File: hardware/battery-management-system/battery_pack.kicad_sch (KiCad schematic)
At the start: 24 parts, among them J1 CELLS, J2 Charge, J3 Discharge, J4 VBAT_DISCHARGE, Q1 DMN3404L, Q2 TJ40S04M3L, Q3 TJ40S04M3L, Q4 DMN3404L, U11 STC3100

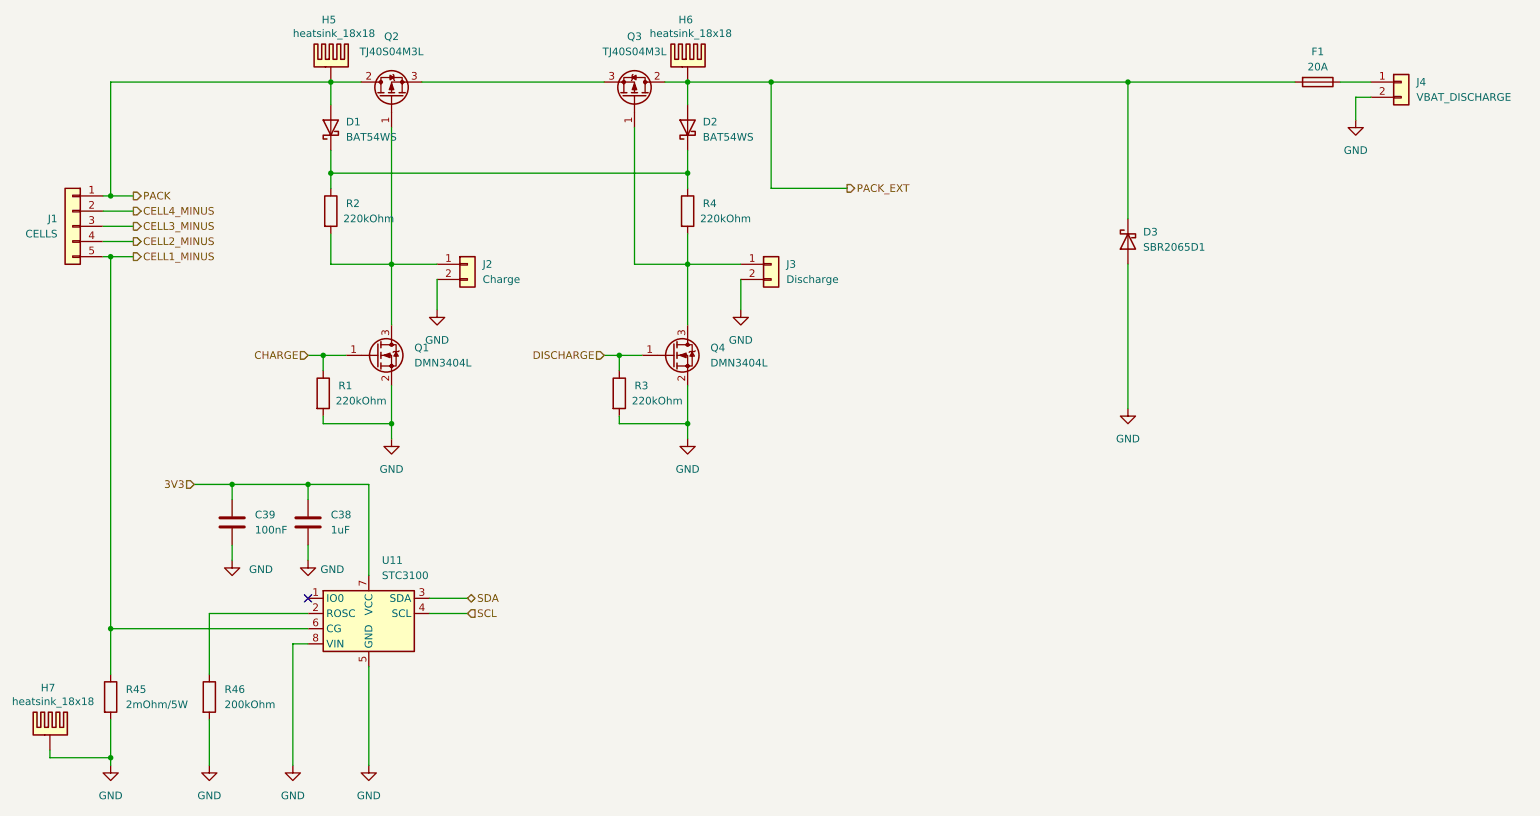
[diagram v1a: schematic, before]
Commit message: add snubber circuit
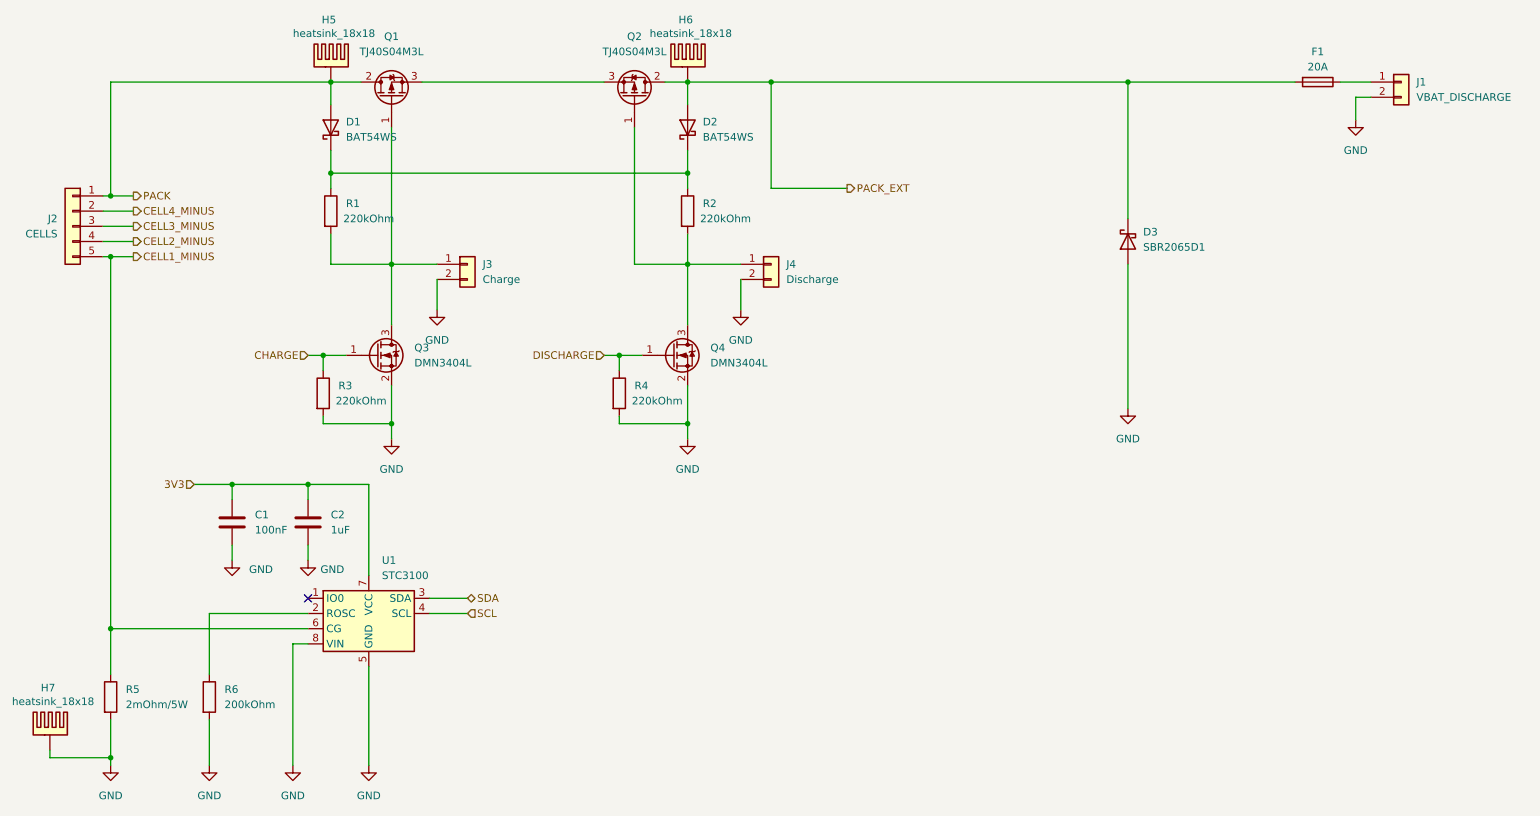
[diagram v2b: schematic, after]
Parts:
- renumbered C39 to C1, C38 to C2, J4 to J1, J1 to J2, J2 to J3, J3 to J4, Q2 to Q1, Q3 to Q2, Q1 to Q3, R2 to R1, R4 to R2, R1 to R3, R3 to R4, R45 to R5, R46 to R6, U11 to U1
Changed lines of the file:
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@@
 		(dnp no)
 		(fields_autoplaced yes)
-		(property "Reference" "J4"
+		(property "Reference" "J1"
 			(at 266.7 44.45 0)
 			(effects
@@
 			(project "battery-management-system"
 				(path "/5272f0ff-3069-41a9-bca2-80beede8b4b2/31b87c35-c096-4dc0-8978-834bec283b57"
-					(reference "J4")
+					(reference "J1")
 					(unit 1)
 				)
@@
 		(dnp no)
 		(fields_autoplaced yes)
-		(property "Reference" "#PWR09"
+		(property "Reference" "#PWR07"
 			(at 153.67 88.9 0)
 			(effects
@@
 			(project "battery-management-system"
 				(path "/5272f0ff-3069-41a9-bca2-80beede8b4b2/31b87c35-c096-4dc0-8978-834bec283b57"
-					(reference "#PWR09")
+					(reference "#PWR07")
 					(unit 1)
 				)
@@
 		(dnp no)
 		(fields_autoplaced yes)
-		(property "Reference" "#PWR071"
+		(property "Reference" "#PWR08"
 			(at 218.44 105.41 0)
 			(effects
@@
 			(project "battery-management-system"
 				(path "/5272f0ff-3069-41a9-bca2-80beede8b4b2/31b87c35-c096-4dc0-8978-834bec283b57"
-					(reference "#PWR071")
+					(reference "#PWR08")
 					(unit 1)
 				)
@@
 		(dnp no)
 		(fields_autoplaced yes)
-		(property "Reference" "C39"
+		(property "Reference" "C1"
 			(at 72.39 116.8399 0)
 			(effects
@@
 			(project "battery-management-system"
 				(path "/5272f0ff-3069-41a9-bca2-80beede8b4b2/31b87c35-c096-4dc0-8978-834bec283b57"
-					(reference "C39")
+					(reference "C1")
 					(unit 1)
 				)
@@
 		(dnp no)
 		(fields_autoplaced yes)
-		(property "Reference" "J2"
+		(property "Reference" "J3"
 			(at 110.49 74.93 0)
 			(effects
@@
 			(project "battery-management-system"
 				(path "/5272f0ff-3069-41a9-bca2-80beede8b4b2/31b87c35-c096-4dc0-8978-834bec283b57"
-					(reference "J2")
+					(reference "J3")
 					(unit 1)
 				)
@@
 		(on_board yes)
 		(dnp no)
-		(property "Reference" "R3"
+		(property "Reference" "R4"
 			(at 135.89 95.2499 0)
 			(effects
@@
 			(project "battery-management-system"
 				(path "/5272f0ff-3069-41a9-bca2-80beede8b4b2/31b87c35-c096-4dc0-8978-834bec283b57"
-					(reference "R3")
+					(reference "R4")
 					(unit 1)
 				)
@@
 		(dnp no)
 		(fields_autoplaced yes)
-		(property "Reference" "U11"
+		(property "Reference" "U1"
 			(at 93.6341 124.46 0)
 			(effects
@@
 			(project "battery-management-system"
 				(path "/5272f0ff-3069-41a9-bca2-80beede8b4b2/31b87c35-c096-4dc0-8978-834bec283b57"
-					(reference "U11")
+					(reference "U1")
 					(unit 1)
 				)
@@
 		(dnp no)
 		(fields_autoplaced yes)
-		(property "Reference" "#PWR08"
+		(property "Reference" "#PWR010"
 			(at 144.78 110.49 0)
 			(effects
@@
 			(project "battery-management-system"
 				(path "/5272f0ff-3069-41a9-bca2-80beede8b4b2/31b87c35-c096-4dc0-8978-834bec283b57"
-					(reference "#PWR08")
+					(reference "#PWR010")
 					(unit 1)
 				)
@@
 		(on_board yes)
 		(dnp no)
-		(property "Reference" "R46"
+		(property "Reference" "R6"
 			(at 67.31 146.0499 0)
 			(effects
@@
 			(project "battery-management-system"
 				(path "/5272f0ff-3069-41a9-bca2-80beede8b4b2/31b87c35-c096-4dc0-8978-834bec283b57"
-					(reference "R46")
+					(reference "R6")
 					(unit 1)
 				)
@@
 		(dnp no)
 		(fields_autoplaced yes)
-		(property "Reference" "#PWR06"
+		(property "Reference" "#PWR09"
 			(at 95.25 110.49 0)
 			(effects
@@
 			(project "battery-management-system"
 				(path "/5272f0ff-3069-41a9-bca2-80beede8b4b2/31b87c35-c096-4dc0-8978-834bec283b57"
-					(reference "#PWR06")
+					(reference "#PWR09")
 					(unit 1)
 				)
@@
 		(dnp no)
 		(fields_autoplaced yes)
-		(property "Reference" "R45"
+		(property "Reference" "R5"
 			(at 50.8 146.0499 0)
 			(effects
@@
 			(project "battery-management-system"
 				(path "/5272f0ff-3069-41a9-bca2-80beede8b4b2/31b87c35-c096-4dc0-8978-834bec283b57"
-					(reference "R45")
+					(reference "R5")
 					(unit 1)
 				)
@@
 		(dnp no)
 		(fields_autoplaced yes)
-		(property "Reference" "#PWR05"
+		(property "Reference" "#PWR013"
 			(at 48.26 165.1 0)
 			(effects
@@
 			(project "battery-management-system"
 				(path "/5272f0ff-3069-41a9-bca2-80beede8b4b2/31b87c35-c096-4dc0-8978-834bec283b57"
-					(reference "#PWR05")
+					(reference "#PWR013")
 					(unit 1)
 				)
@@
 		(on_board yes)
 		(dnp no)
-		(property "Reference" "J1"
+		(property "Reference" "J2"
 			(at 39.37 67.31 0)
 			(effects
@@
 			(project "battery-management-system"
 				(path "/5272f0ff-3069-41a9-bca2-80beede8b4b2/31b87c35-c096-4dc0-8978-834bec283b57"
-					(reference "J1")
+					(reference "J2")
 					(unit 1)
 				)
@@
 		(on_board yes)
 		(dnp no)
-		(property "Reference" "R2"
+		(property "Reference" "R1"
 			(at 87.63 64.7699 0)
 			(effects
@@
 			(project "battery-management-system"
 				(path "/5272f0ff-3069-41a9-bca2-80beede8b4b2/31b87c35-c096-4dc0-8978-834bec283b57"
-					(reference "R2")
+					(reference "R1")
 					(unit 1)
 				)
@@
 		(dnp no)
 		(fields_autoplaced yes)
-		(property "Reference" "#PWR073"
+		(property "Reference" "#PWR014"
 			(at 64.77 165.1 0)
 			(effects
@@
 			(project "battery-management-system"
 				(path "/5272f0ff-3069-41a9-bca2-80beede8b4b2/31b87c35-c096-4dc0-8978-834bec283b57"
-					(reference "#PWR073")
+					(reference "#PWR014")
 					(unit 1)
 				)
@@
 		(dnp no)
 		(fields_autoplaced yes)
-		(property "Reference" "C38"
+		(property "Reference" "C2"
 			(at 85.09 116.8399 0)
 			(effects
@@
 			(project "battery-management-system"
 				(path "/5272f0ff-3069-41a9-bca2-80beede8b4b2/31b87c35-c096-4dc0-8978-834bec283b57"
-					(reference "C38")
+					(reference "C2")
 					(unit 1)
 				)
@@
 		(dnp no)
 		(fields_autoplaced yes)
-		(property "Reference" "Q3"
+		(property "Reference" "Q2"
 			(at 135.89 36.83 90)
 			(effects
@@
 			(project "battery-management-system"
 				(path "/5272f0ff-3069-41a9-bca2-80beede8b4b2/31b87c35-c096-4dc0-8978-834bec283b57"
-					(reference "Q3")
+					(reference "Q2")
 					(unit 1)
 				)
@@
 		(dnp no)
 		(fields_autoplaced yes)
-		(property "Reference" "#PWR075"
+		(property "Reference" "#PWR016"
 			(at 91.44 165.1 0)
 			(effects
@@
 			(project "battery-management-system"
 				(path "/5272f0ff-3069-41a9-bca2-80beede8b4b2/31b87c35-c096-4dc0-8978-834bec283b57"
-					(reference "#PWR075")
+					(reference "#PWR016")
 					(unit 1)
 				)
@@
 		(dnp no)
 		(fields_autoplaced yes)
-		(property "Reference" "Q2"
+		(property "Reference" "Q1"
 			(at 95.25 36.83 90)
 			(effects
@@
 			(project "battery-management-system"
 				(path "/5272f0ff-3069-41a9-bca2-80beede8b4b2/31b87c35-c096-4dc0-8978-834bec283b57"
-					(reference "Q2")
+					(reference "Q1")
 					(unit 1)
 				)
@@
 		(on_board yes)
 		(dnp no)
-		(property "Reference" "R4"
+		(property "Reference" "R2"
 			(at 147.32 64.7699 0)
 			(effects
@@
 			(project "battery-management-system"
 				(path "/5272f0ff-3069-41a9-bca2-80beede8b4b2/31b87c35-c096-4dc0-8978-834bec283b57"
-					(reference "R4")
+					(reference "R2")
 					(unit 1)
 				)
@@
 		(dnp no)
 		(fields_autoplaced yes)
-		(property "Reference" "#PWR012"
+		(property "Reference" "#PWR05"
 			(at 256.54 57.15 0)
 			(effects
@@
 			(project "battery-management-system"
 				(path "/5272f0ff-3069-41a9-bca2-80beede8b4b2/31b87c35-c096-4dc0-8978-834bec283b57"
-					(reference "#PWR012")
+					(reference "#PWR05")
 					(unit 1)
 				)
@@
 		(on_board yes)
 		(dnp no)
-		(property "Reference" "#PWR076"
+		(property "Reference" "#PWR012"
 			(at 81.28 130.81 0)
 			(effects
@@
 			(project "battery-management-system"
 				(path "/5272f0ff-3069-41a9-bca2-80beede8b4b2/31b87c35-c096-4dc0-8978-834bec283b57"
-					(reference "#PWR076")
+					(reference "#PWR012")
 					(unit 1)
 				)
@@
 		(dnp no)
 		(fields_autoplaced yes)
-		(property "Reference" "Q1"
+		(property "Reference" "Q3"
 			(at 99.06 88.9 0)
 			(effects
@@
 			(project "battery-management-system"
 				(path "/5272f0ff-3069-41a9-bca2-80beede8b4b2/31b87c35-c096-4dc0-8978-834bec283b57"
-					(reference "Q1")
+					(reference "Q3")
 					(unit 1)
 				)
@@
 		(on_board yes)
 		(dnp no)
-		(property "Reference" "#PWR077"
+		(property "Reference" "#PWR011"
 			(at 68.58 130.81 0)
 			(effects
@@
 			(project "battery-management-system"
 				(path "/5272f0ff-3069-41a9-bca2-80beede8b4b2/31b87c35-c096-4dc0-8978-834bec283b57"
-					(reference "#PWR077")
+					(reference "#PWR011")
 					(unit 1)
 				)
@@
 		(dnp no)
 		(fields_autoplaced yes)
-		(property "Reference" "J3"
+		(property "Reference" "J4"
 			(at 161.29 74.93 0)
 			(effects
@@
 			(project "battery-management-system"
 				(path "/5272f0ff-3069-41a9-bca2-80beede8b4b2/31b87c35-c096-4dc0-8978-834bec283b57"
-					(reference "J3")
+					(reference "J4")
 					(unit 1)
 				)
@@
 		(dnp no)
 		(fields_autoplaced yes)
-		(property "Reference" "#PWR074"
+		(property "Reference" "#PWR015"
 			(at 78.74 165.1 0)
 			(effects
@@
 			(project "battery-management-system"
 				(path "/5272f0ff-3069-41a9-bca2-80beede8b4b2/31b87c35-c096-4dc0-8978-834bec283b57"
-					(reference "#PWR074")
+					(reference "#PWR015")
 					(unit 1)
 				)
@@
 		(on_board yes)
 		(dnp no)
-		(property "Reference" "R1"
+		(property "Reference" "R3"
 			(at 86.36 95.2499 0)
 			(effects
@@
 			(project "battery-management-system"
 				(path "/5272f0ff-3069-41a9-bca2-80beede8b4b2/31b87c35-c096-4dc0-8978-834bec283b57"
-					(reference "R1")
+					(reference "R3")
 					(unit 1)
 				)
@@
 		(dnp no)
 		(fields_autoplaced yes)
-		(property "Reference" "#PWR07"
+		(property "Reference" "#PWR06"
 			(at 102.87 88.9 0)
 			(effects
@@
 			(project "battery-management-system"
 				(path "/5272f0ff-3069-41a9-bca2-80beede8b4b2/31b87c35-c096-4dc0-8978-834bec283b57"
-					(reference "#PWR07")
-					(unit 1)
-				)
+					(reference "#PWR06")
+					(unit 1)
+				)

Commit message: update symbols from library
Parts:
- H5, H6, H7: Mouser Part Number (none) -> 490-HSB06-181810
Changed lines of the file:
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@@
+			)
+		)
+		(property "Mouser Part Number" "490-HSB06-181810"
+			(at 38.608 146.558 0)
+			(effects
+				(font
+					(size 1.27 1.27)
+				)
+				(hide yes)
 			)
 		)
@@
 			)
 		)
+		(property "Mouser Part Number" "490-HSB06-181810"
+			(at 145.288 34.798 0)
+			(effects
+				(font
+					(size 1.27 1.27)
+				)
+				(hide yes)
+			)
+		)
 		(pin "PAD"
 		)
@@
 			(at 85.598 34.798 0)
 			(effects
+				(font
+					(size 1.27 1.27)
+				)
+				(hide yes)
+			)
+		)
+		(property "Mouser Part Number" "490-HSB06-181810"
+			(at 85.598 34.798 0)
+			(effects

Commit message: update symbols from library
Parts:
- C1: Mouser Part Number (none) -> 581-KGM15BR71H104KM
- C2: Mouser Part Number (none) -> 963-UMK107BJ105KA-T
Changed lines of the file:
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@@
+			)
+		)
+		(property "Mouser Part Number" "581-KGM15BR71H104KM"
+			(at 86.106 116.84 0)
+			(effects
+				(font
+					(size 1.27 1.27)
+				)
+				(hide yes)
 			)
 		)
@@
 			(at 98.806 116.84 0)
 			(effects
+				(font
+					(size 1.27 1.27)
+				)
+				(hide yes)
+			)
+		)
+		(property "Mouser Part Number" "963-UMK107BJ105KA-T"
+			(at 98.806 116.84 0)
+			(effects

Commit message: update symbols from library
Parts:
- R1, R2, R3, R4: Mouser Part Number (none) -> 71-CRCW0603-220K-E3
- R6: Mouser Part Number (none) -> 667-ERA-3AEB204V
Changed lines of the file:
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@@
+			)
+		)
+		(property "Mouser Part Number" "71-CRCW0603-220K-E3"
+			(at 115.57 95.25 0)
+			(effects
+				(font
+					(size 1.27 1.27)
+				)
+				(hide yes)
 			)
 		)
@@
 			)
 		)
+		(property "Mouser Part Number" "667-ERA-3AEB204V"
+			(at 46.99 146.05 0)
+			(effects
+				(font
+					(size 1.27 1.27)
+				)
+				(hide yes)
+			)
+		)
 		(pin "2"
 		)
@@
 			)
 		)
+		(property "Mouser Part Number" "71-CRCW0603-220K-E3"
+			(at 67.31 64.77 0)
+			(effects
+				(font
+					(size 1.27 1.27)
+				)
+				(hide yes)
+			)
+		)
 		(pin "1"
 		)
@@
 			)
 		)
+		(property "Mouser Part Number" "71-CRCW0603-220K-E3"
+			(at 127 64.77 0)
+			(effects
+				(font
+					(size 1.27 1.27)
+				)
+				(hide yes)
+			)
+		)
 		(pin "1"
 		)
@@
 			(at 66.04 95.25 0)
 			(effects
+				(font
+					(size 1.27 1.27)
+				)
+				(hide yes)
+			)
+		)
+		(property "Mouser Part Number" "71-CRCW0603-220K-E3"
+			(at 66.04 95.25 0)
+			(effects

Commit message: update symbols from library
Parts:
- D1, D2: Mouser Part Number (none) -> 637-BAT54WS
- D3: Mouser Part Number (none) -> 621-SBR2065D1-13
- Q1, Q2: Mouser Part Number (none) -> 757-TJ40S04M3LT6L1NQ
- Q3, Q4: Mouser Part Number (none) -> 621-DMN3404L-7
- R5: Mouser Part Number (none) -> 660-TLR3APSDTE2L00F7
- U1: Mouser Part Number (none) -> 511-STC3100IST
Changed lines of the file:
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@@
+			)
+		)
+		(property "Mouser Part Number" "637-BAT54WS"
+			(at 90.17 53.594 0)
+			(effects
+				(font
+					(size 1.27 1.27)
+				)
+				(hide yes)
 			)
 		)
@@
 			)
 		)
+		(property "Mouser Part Number" "621-SBR2065D1-13"
+			(at 223.52 69.596 0)
+			(effects
+				(font
+					(size 1.27 1.27)
+				)
+				(hide yes)
+			)
+		)
 		(pin "1"
 		)
@@
 			)
 		)
+		(property "Mouser Part Number" "511-STC3100IST"
+			(at 91.44 134.62 0)
+			(effects
+				(font
+					(size 1.27 1.27)
+				)
+				(hide yes)
+			)
+		)
 		(pin "7"
 		)
@@
 			)
 		)
+		(property "Mouser Part Number" "660-TLR3APSDTE2L00F7"
+			(at 30.48 146.05 0)
+			(effects
+				(font
+					(size 1.27 1.27)
+				)
+				(hide yes)
+			)
+		)
 		(pin "1"
 		)
@@
 			)
 		)
+		(property "Mouser Part Number" "757-TJ40S04M3LT6L1NQ"
+			(at 135.89 46.99 0)
+			(effects
+				(font
+					(size 1.27 1.27)
+				)
+				(hide yes)
+			)
+		)
 		(pin "1"
 		)
@@
 			)
 		)
+		(property "Mouser Part Number" "757-TJ40S04M3LT6L1NQ"
+			(at 95.25 46.99 0)
+			(effects
+				(font
+					(size 1.27 1.27)
+				)
+				(hide yes)
+			)
+		)
 		(pin "1"
 		)
@@
 			)
 		)
+		(property "Mouser Part Number" "621-DMN3404L-7"
+			(at 139.7 95.25 0)
+			(effects
+				(font
+					(size 1.27 1.27)
+				)
+				(hide yes)
+			)
+		)
 		(pin "1"
 		)
@@
 			)
 		)
+		(property "Mouser Part Number" "621-DMN3404L-7"
+			(at 90.17 95.25 0)
+			(effects
+				(font
+					(size 1.27 1.27)
+				)
+				(hide yes)
+			)
+		)
 		(pin "1"
 		)
@@
 			(effects
 				(font
+					(size 1.27 1.27)
+				)
+				(hide yes)
+			)
+		)
+		(property "Mouser Part Number" "637-BAT54WS"
+			(at 149.86 53.594 0)
+			(effects
+				(font
